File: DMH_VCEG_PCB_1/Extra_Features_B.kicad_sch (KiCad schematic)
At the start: 46 parts, among them J25 Conn_01x10_PinHeader, J26 Conn_01x10_PinHeader, Q8 BC548, SW2 SW_DPDT_x2, SW5 SW_SPDT_321_OnOff, U10 TL074, U12 40106, U17 TL074, U20 4001

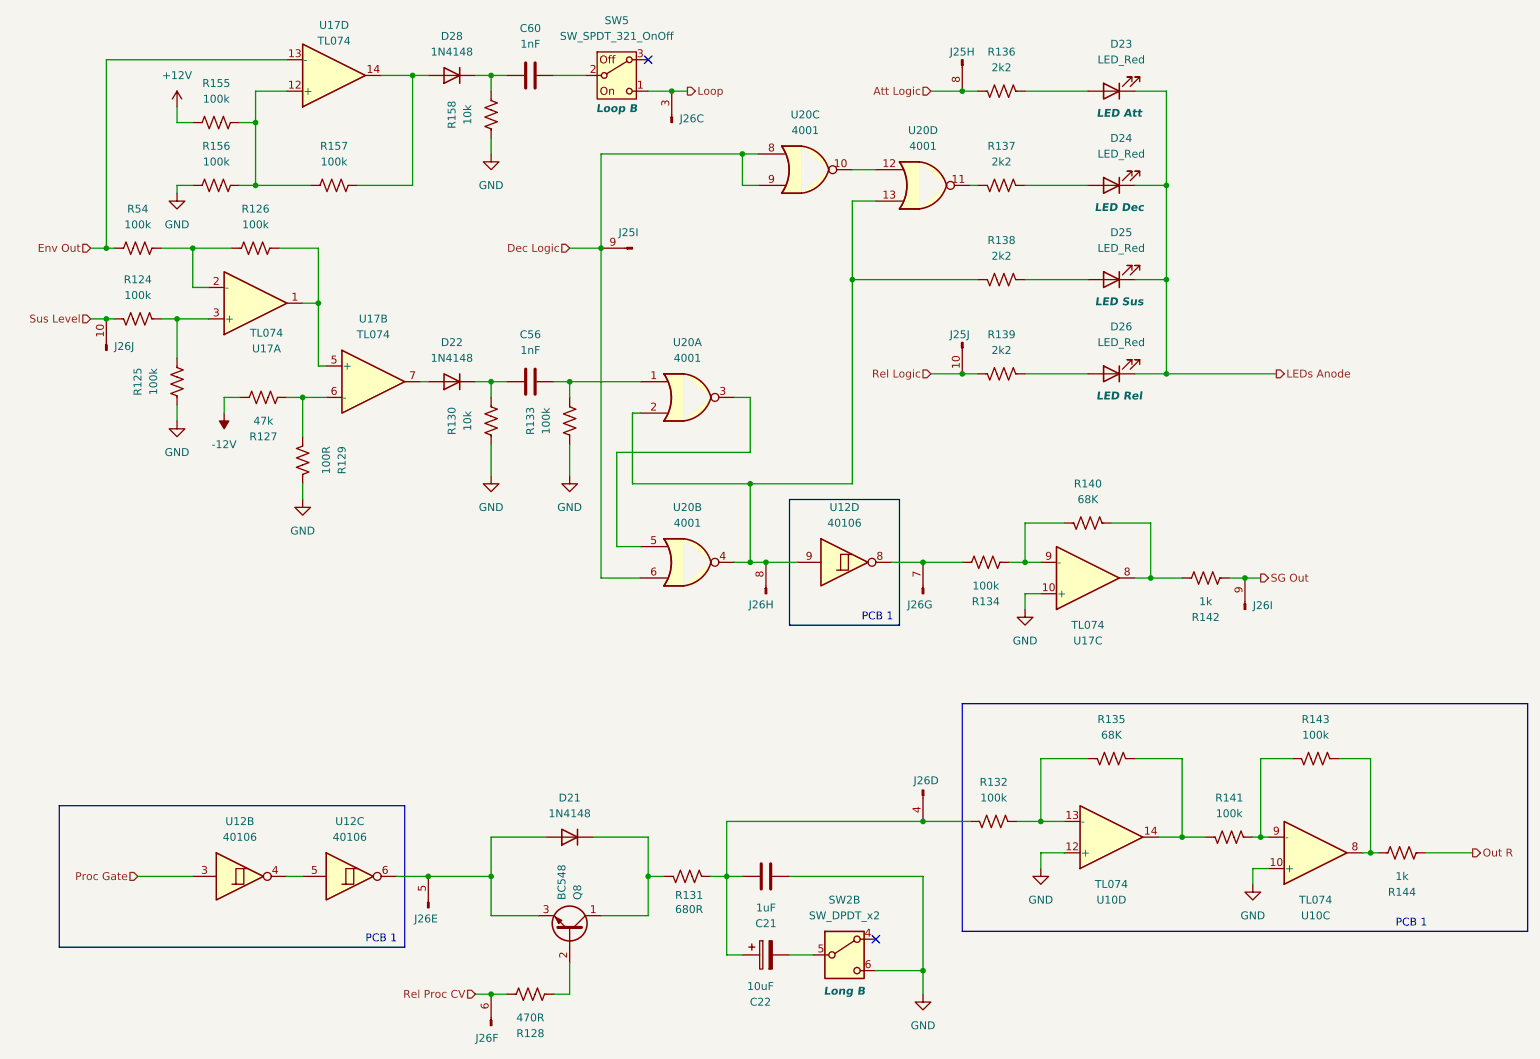
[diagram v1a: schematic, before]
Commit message: Copied Manual Gate circuit to PCB 1 schematic
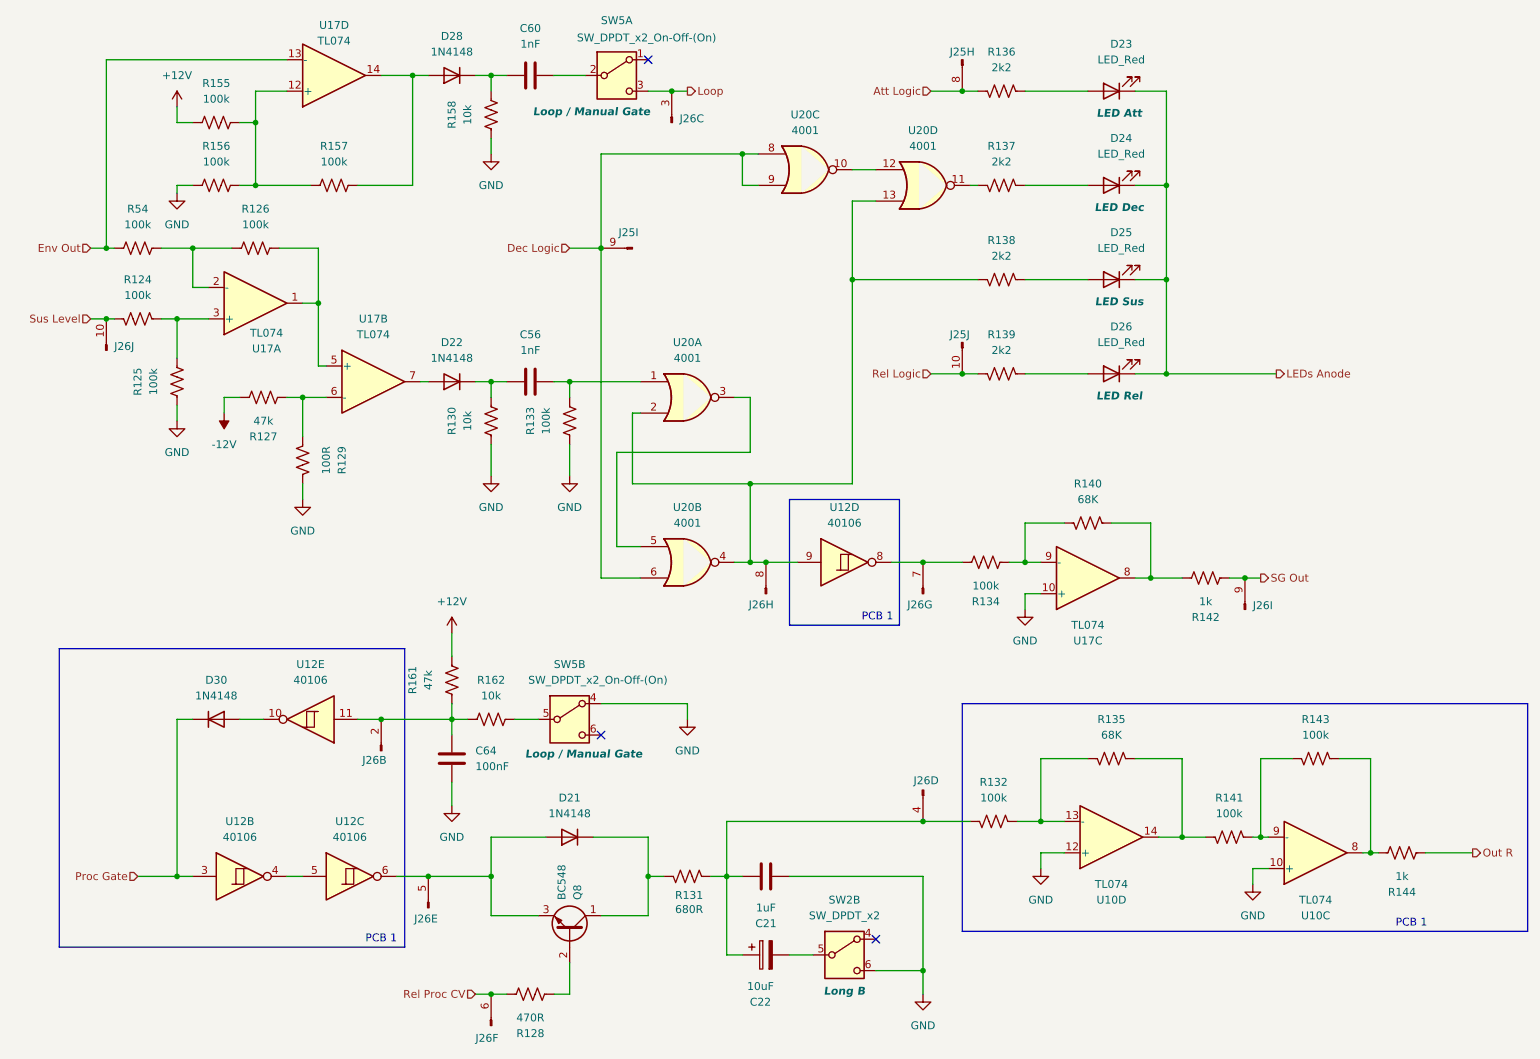
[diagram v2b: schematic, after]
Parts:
- removed SW5: SW_SPDT_321_OnOff, SynthStuff:Toggle_Switch_TE, symbol SynthStuff:SW_SPDT_321_OnOff
- added C64: 100nF, Capacitor_THT:C_Disc_D4.3mm_W1.9mm_P5.00mm, symbol Device:C
- added D30: 1N4148, Diode_THT:D_DO-35_SOD27_P7.62mm_Horizontal, symbol Diode:1N4148
- added unit 2 of J26
- added R161: 47k, Resistor_THT:R_Axial_DIN0207_L6.3mm_D2.5mm_P7.62mm_Horizontal, symbol Device:R_US
- added R162: 10k, Resistor_THT:R_Axial_DIN0207_L6.3mm_D2.5mm_P7.62mm_Horizontal, symbol Device:R_US
- added SW5: SW_DPDT_x2_On-Off-(On), symbol Switch:SW_DPDT_x2
- added unit 5 of U12
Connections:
- net +12V: now also R161.1
- net GND: now also C64.2, SW5.4 (A)
- net Loop: now also SW5.3 (C)
- net Proc Gate: now also D30.1 (K)
- net at C60.2: now also SW5.2 (B)
- new net: R162.1, SW5.5 (B)
- new net: C64.1, J26.2 (Pin_2), R161.2, R162.2, U12.11
- new net: D30.2 (A), U12.10
- no-connect marks 2 -> 3

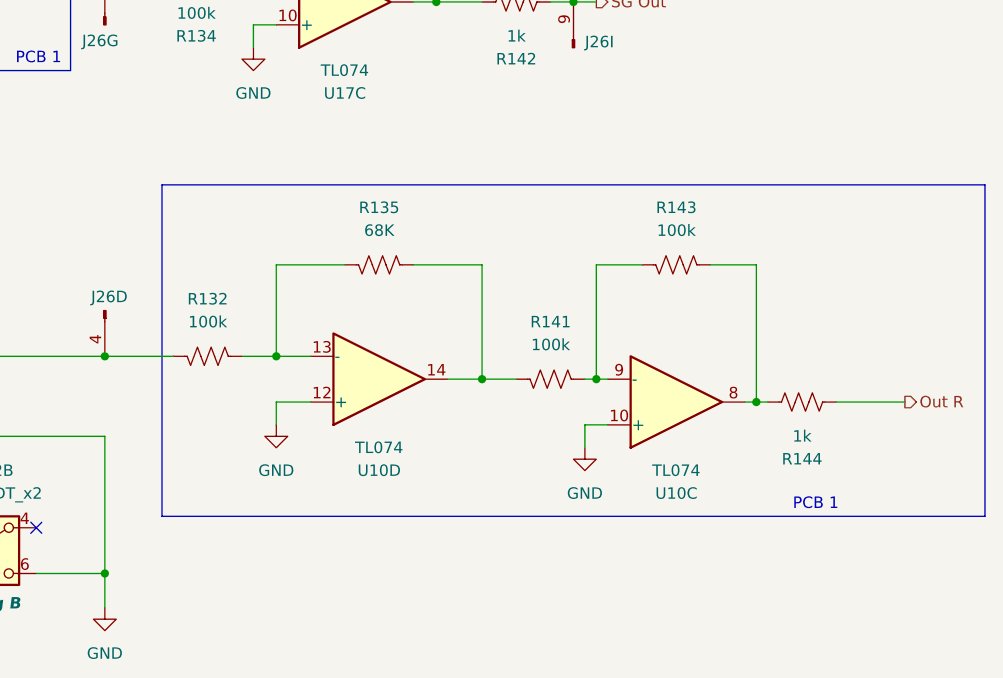
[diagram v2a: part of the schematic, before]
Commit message: Added Output attenuation circuit
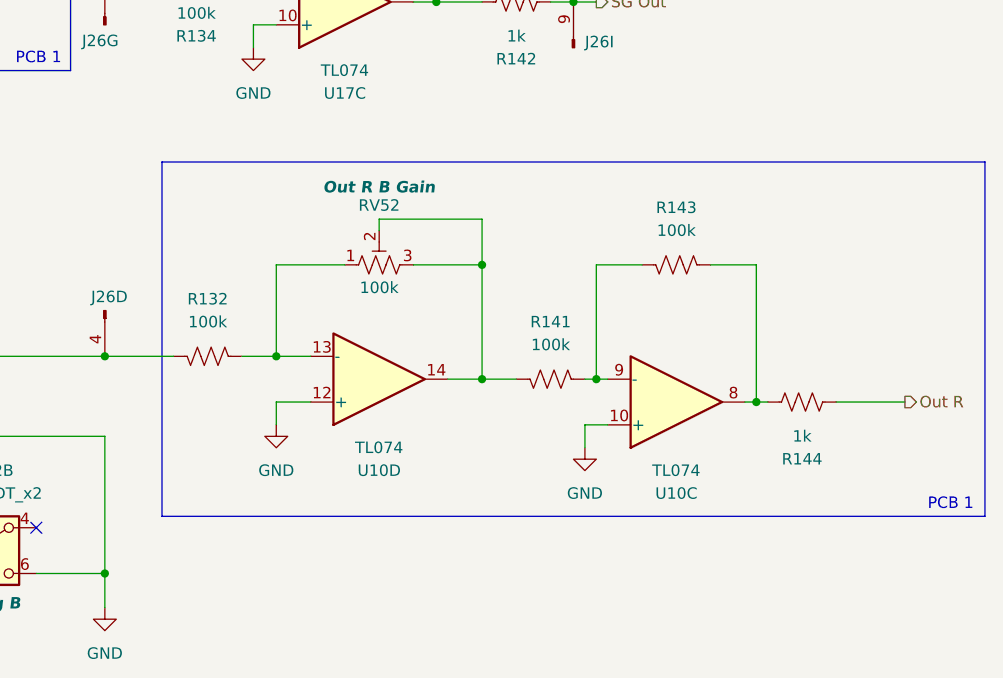
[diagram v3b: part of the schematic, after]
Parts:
- removed R135: 68K, Resistor_THT:R_Axial_DIN0207_L6.3mm_D2.5mm_P7.62mm_Horizontal, symbol Device:R_US
- added RV52: 100k, Potentiometer_THT:Potentiometer_Bourns_3296X_Horizontal, symbol Device:R_Potentiometer_Trim_US
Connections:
- net at R132.2, U10.13 (-): now also RV52.1
- net at R141.1, U10.14: now also RV52.2, RV52.3
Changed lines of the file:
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@@
 	)
 	(rectangle
-		(start 165.1 124.46)
+		(start 165.1 121.92)
 		(end 256.54 161.29)
 		(stroke
@@
 	(text "PCB 1"
 		(exclude_from_sim no)
-		(at 237.744 160.02 0)
+		(at 252.73 160.02 0)
 		(effects
 			(font
@@
 	)
 	(junction
+		(at 200.66 133.35)
+		(diameter 0)
+		(color 0 0 0 0)
+	)
+	(junction
 		(at 88.9 171.45)
 		(diameter 0)
@@
 	(wire
 		(pts
+			(xy 189.23 128.27) (xy 200.66 128.27)
+		)
+		(stroke
+			(width 0)
+			(type default)
+		)
+	)
+	(wire
+		(pts
 			(xy 88.9 33.02) (xy 88.9 35.56)
 		)
@@
 	(wire
 		(pts
+			(xy 200.66 128.27) (xy 200.66 133.35)
+		)
+		(stroke
+			(width 0)
+			(type default)
+		)
+	)
+	(wire
+		(pts
 			(xy 193.04 40.64) (xy 198.12 40.64)
 		)
@@
 	(wire
 		(pts
+			(xy 189.23 129.54) (xy 189.23 128.27)
+		)
+		(stroke
+			(width 0)
+			(type default)
+		)
+	)
+	(wire
+		(pts
 			(xy 158.75 101.6) (xy 165.1 101.6)
 		)
@@
 	)
 	(symbol
-		(lib_id "Device:R_US")
-		(at 189.23 133.35 90)
-		(mirror x)
-		(unit 1)
-		(exclude_from_sim no)
-		(in_bom yes)
-		(on_board yes)
-		(dnp no)
-		(property "Reference" "R135"
-			(at 189.23 127 90)
-			(effects
-				(font
-					(size 1.27 1.27)
-				)
-			)
-		)
-		(property "Value" "68K"
-			(at 189.23 129.54 90)
-			(effects
-				(font
-					(size 1.27 1.27)
-				)
-			)
-		)
-		(property "Footprint" "Resistor_THT:R_Axial_DIN0207_L6.3mm_D2.5mm_P7.62mm_Horizontal"
-			(at 189.484 134.366 90)
-			(effects
-				(font
-					(size 1.27 1.27)
-				)
-				(hide yes)
-			)
-		)
-		(property "Datasheet" "~"
-			(at 189.23 133.35 0)
-			(effects
-				(font
-					(size 1.27 1.27)
-				)
-				(hide yes)
-			)
-		)
-		(property "Description" "Resistor, US symbol"
-			(at 189.23 133.35 0)
-			(effects
-				(font
-					(size 1.27 1.27)
-				)
-				(hide yes)
-			)
-		)
-		(pin "2"
-		)
-		(pin "1"
-		)
-		(instances
-			(project "DMH_VCEG_PCB_1"
-				(path "/58f4306d-5387-4983-bb08-41a2313fd315/5112ef52-02ff-4071-9179-b1c0d55d0b73"
-					(reference "R135")
-					(unit 1)
-				)
-			)
-		)
-	)
-	(symbol
 		(lib_id "SynthStuff:Conn_01x10_PinHeader")
 		(at 133.35 106.68 90)
@@
 				)
 			)
+		)
+	)
+	(symbol
+		(lib_id "Device:R_Potentiometer_Trim_US")
+		(at 189.23 133.35 90)
+		(unit 1)
+		(exclude_from_sim no)
+		(in_bom yes)
+		(on_board yes)
+		(dnp no)
+		(property "Reference" "RV52"
+			(at 189.23 126.746 90)
+			(effects
+				(font
+					(size 1.27 1.27)
+				)
+			)
+		)
+		(property "Value" "100k"
+			(at 189.23 135.89 90)
+			(effects
+				(font
+					(size 1.27 1.27)
+				)
+			)
+		)
+		(property "Footprint" "Potentiometer_THT:Potentiometer_Bourns_3296X_Horizontal"
+			(at 189.23 133.35 0)
+			(effects
+				(font
+					(size 1.27 1.27)
+				)
+				(hide yes)
+			)
+		)
+		(property "Datasheet" "~"
+			(at 189.23 133.35 0)
+			(effects
+				(font
+					(size 1.27 1.27)
+				)
+				(hide yes)
+			)
+		)
+		(property "Description" "Trim-potentiometer, US symbol"
+			(at 189.23 133.35 0)
+			(effects
+				(font
+					(size 1.27 1.27)
+				)
+				(hide yes)
+			)
+		)
+		(property "Function" "Out R B Gain"
+			(at 189.23 124.714 90)
+			(effects
+				(font
+					(size 1.27 1.27)
+					(thickness 0.254)
+					(bold yes)
+					(italic yes)
+				)
+			)
+		)
+		(pin "2"
+		)
+		(pin "1"
+		)
+		(pin "3"
+		)
+		(instances
+			(project "DMH_VCEG_PCB_1"
+				(path "/58f4306d-5387-4983-bb08-41a2313fd315/5112ef52-02ff-4071-9179-b1c0d55d0b73"
+					(reference "RV52")
+					(unit 1)
+				)
+			)

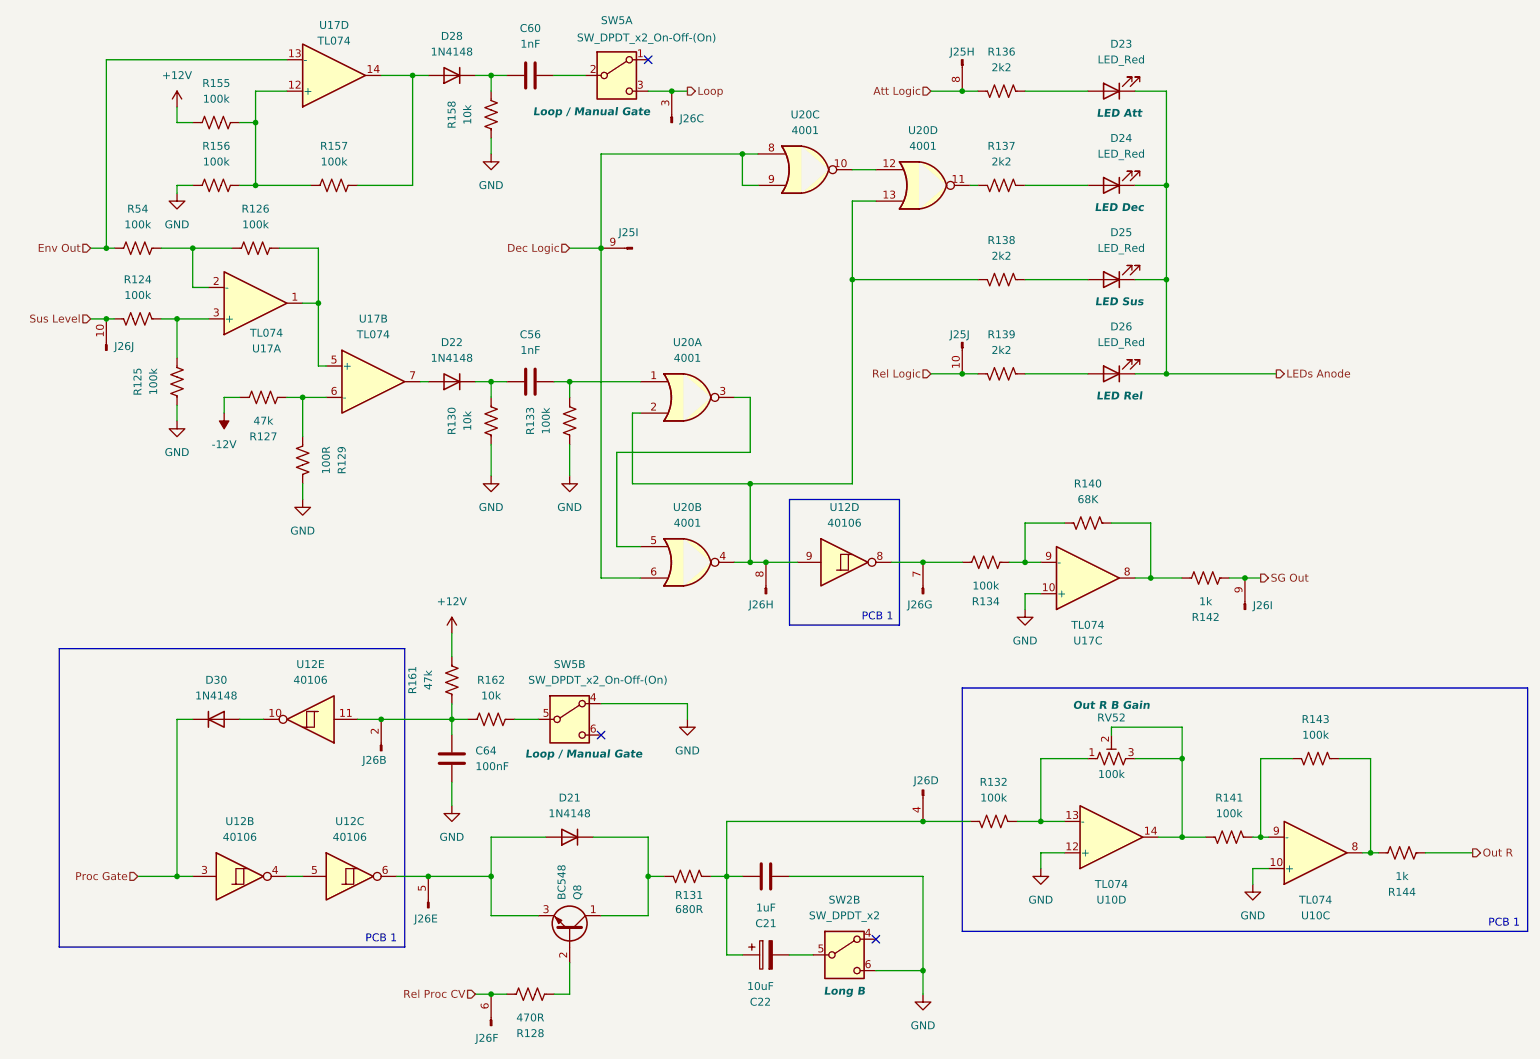
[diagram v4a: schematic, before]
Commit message: Copied circuit A to B
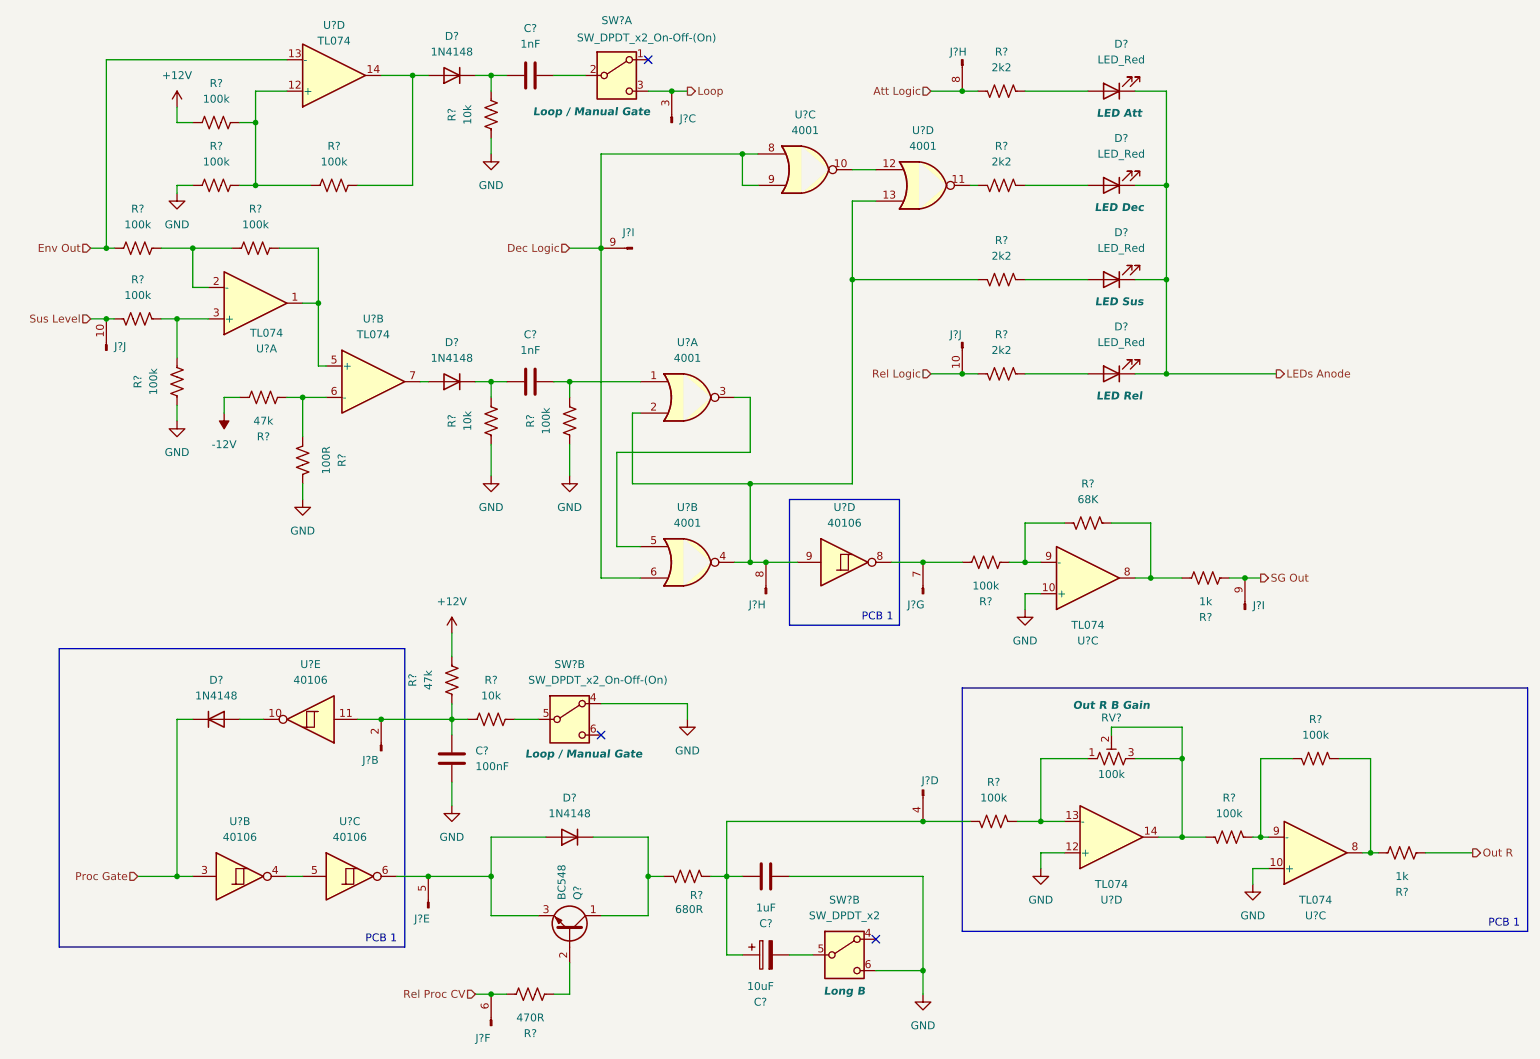
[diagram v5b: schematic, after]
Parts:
- renumbered C21 to C?, C22 to C?, C60 to C?, C64 to C?, C56 to C?, D26 to D?, D28 to D?, D21 to D?, D23 to D?, D30 to D?, D24 to D?, D25 to D?, D22 to D?, J26 to J?, J25 to J?, Q8 to Q?, R162 to R?, R143 to R?, R125 to R?, R136 to R?, R130 to R?, R157 to R?, R138 to R?, R158 to R?, R155 to R?, R129 to R?, R141 to R?, R126 to R?, R133 to R?, R54 to R?, R132 to R?, R134 to R?, R131 to R?, R161 to R?, R142 to R?, R128 to R?, R137 to R?, R156 to R?, R139 to R?, R124 to R?, R144 to R?, R127 to R?, R140 to R?, RV52 to RV?, SW5 to SW?, SW2 to SW?, U17 to U?, U12 to U?, U20 to U?, U10 to U?
